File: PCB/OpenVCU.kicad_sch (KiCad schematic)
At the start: 25 parts, among them U1 STM32H743VIT6, Y1 ABM8-8.000MHZ-18-D1X-T3, Y2 CM315D32768DZFT

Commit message: Root: delete orphan PWR_FLAG legend block, 21 stray no_connect markers
The three PWR_FLAGs (#FLG01-03) sat stacked on three power symbols
(#PWR094-096) at y=191.77 in empty space, isolated from the circuit.
KiCad resolved them into the net containing U1 pin 43 (PE13/PWM3) and
U1 pin 68 (PA9/VBUS_SENSE), which put a power-output pin on those nets
and produced 2 bogus pin_to_pin errors.

Also removed 21 no_connect markers that floated in empty space below
the MCU (y=160..279), including one duplicated marker at (138.43,71.12).
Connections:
- no-connect marks 41 -> 19

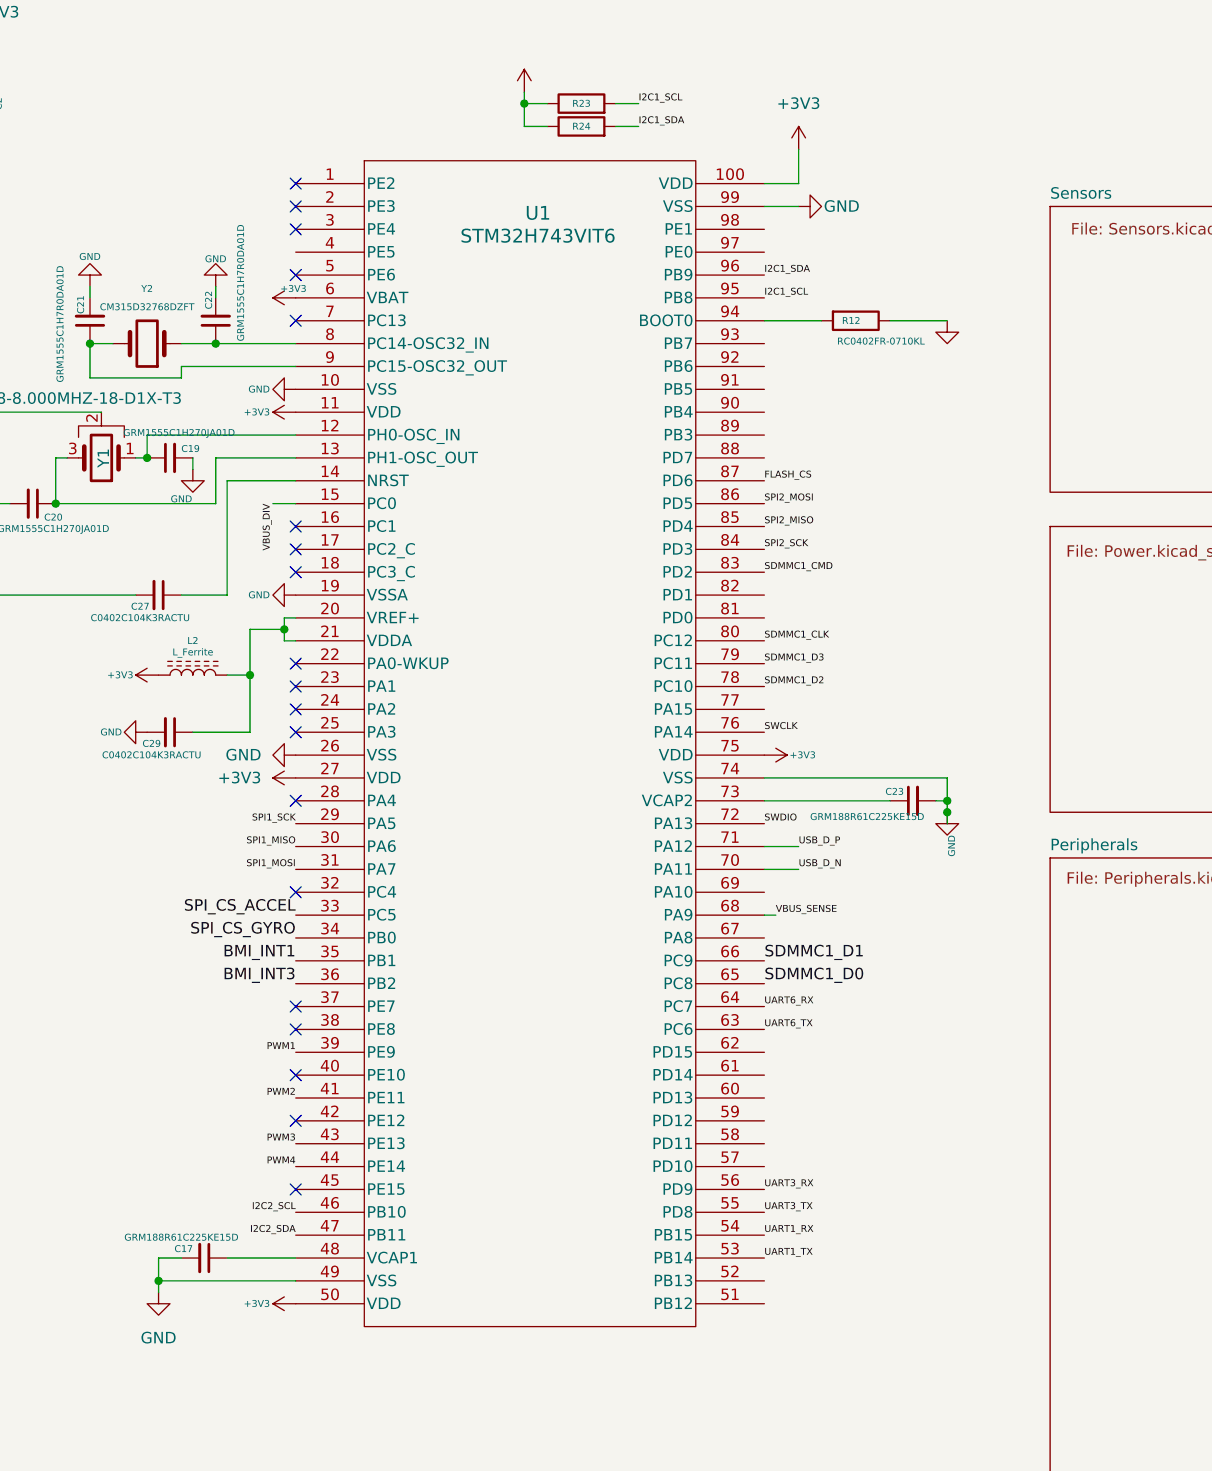
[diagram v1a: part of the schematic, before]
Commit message: Peripherals+root: SWD header, GPIO expansion, PWM output stage, LED/BUZZ/BARO_INT
Peripherals (PCB/Peripherals.kicad_sch):
- J7 (CONN-5) is a proper SWD header: +3V3 / SWDIO / SWCLK / NRST / GND,
  first three exported as hierarchical labels matching the existing root sheet pins.
- J8 (CONN-2x6) expansion header: +3V3, +5V, GND, GND, GPIO_A0..GPIO_A7.
  GPIO_A0..A7 are hierarchical labels on new left-edge sheet pins.
- PWM output stage PWMn -> 100R (R21/R2/R7/R15) -> PWMn_R -> J9 (motor header),
  with the existing 10k R20/R19/R18/R17 as pull-downs on PWMn_R.
- J10 BUZZ and J11 LED exported as hierarchical labels; J4.5 spare TELEM pad -> GND.
- Removed 6 duplicate wires, 4 dead SWDIO/SWCLK labels, 2 floating power symbols.

Root (PCB/OpenVCU.kicad_sch):
- GPIO_A0..A7 on U1.1/2/3/37/22/23/24/28, BUZZ on U1.90 (PB4/TIM16_CH1),
  LED on U1.34 (PB0), BARO_INT on U1.88 (PD7/EXTI7); stale SPI_CS_GYRO and
  BMI_INT3 references cleared.
- 20 no_connect markers added on reserved/spare MCU pins.
- 11 new sheet pins + matching labels on the left edge of the Peripherals sheet box,
  plus NRST at (222.25,135.89).

Library (PCB/OpenVCU.kicad_sym):
- CONN-2x6 pads 7..12 moved to x=+11.43 so the 2x6 header has two columns.

ERC: 282 -> 249 (49 errors, 200 warnings).
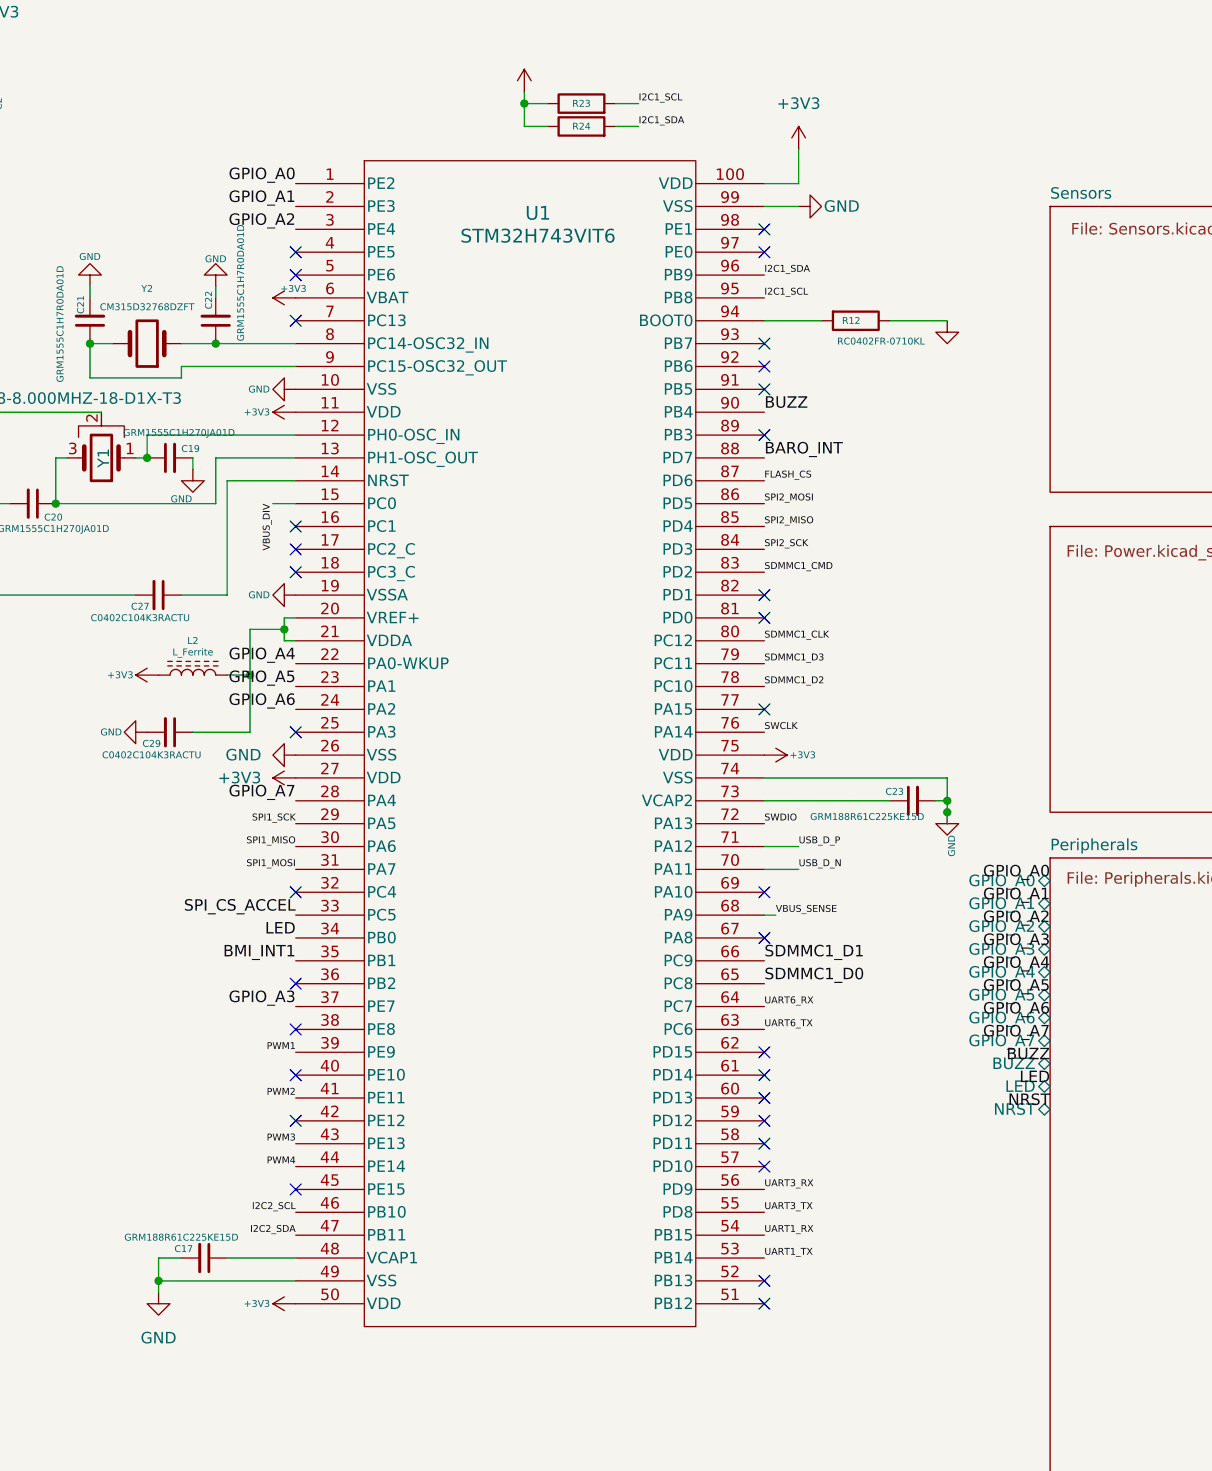
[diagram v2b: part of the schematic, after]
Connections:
- net BARO_INT: now also U1.88 (PD7)
- net GPIO_A0: now reaches U1.1 (PE2)
- net GPIO_A1: now reaches U1.2 (PE3)
- net GPIO_A4: now reaches U1.22 (PA0-WKUP)
- net GPIO_A5: now reaches U1.23 (PA1)
- net GPIO_A6: now reaches U1.24 (PA2)
- net GPIO_A7: now reaches U1.28 (PA4)
- net GPIO_A2: now reaches U1.3 (PE4)
- net GPIO_A3: now reaches U1.37 (PE7)
- net BUZZ: now reaches U1.90 (PB4)
- net BMI_INT3: no longer names the net of U1.36 (PB2)
- net SPI_CS_GYRO renamed LED
- no-connect marks 19 -> 32
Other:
- sheet Peripherals ports: added BUZZ, GPIO_A0, GPIO_A1, GPIO_A2, GPIO_A3, GPIO_A4, GPIO_A5, GPIO_A6, GPIO_A7, LED, NRST; removed none
